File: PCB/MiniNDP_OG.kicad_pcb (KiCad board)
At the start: 2 copper layers, 60 x 34 mm, 27 parts, among them J1 Conn_02x20_Odd_Even, U1 HC161, U2 HC161, U3 HC161, U4 HC138, U5 HC574, U6 AS6C4008, U7 1G32, U8 1G79

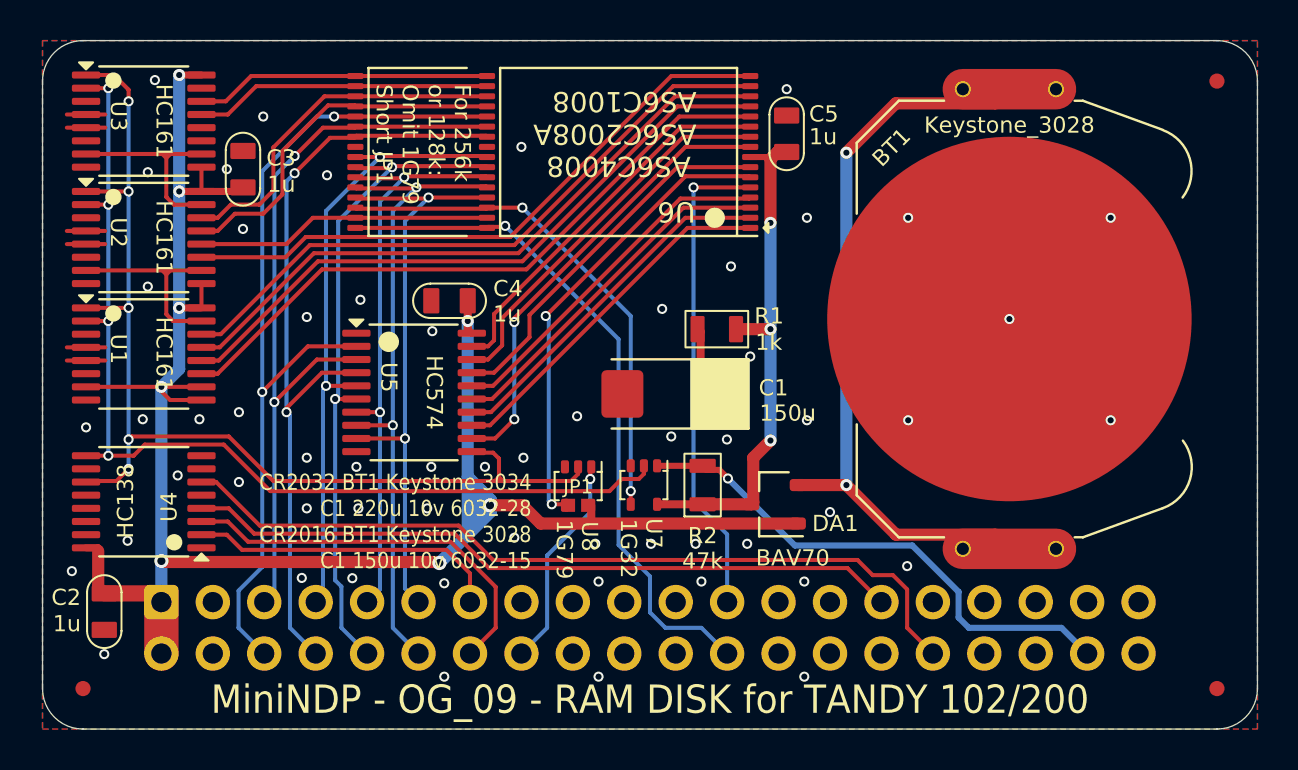
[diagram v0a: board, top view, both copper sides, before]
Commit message: minindp og orient bav70 for easier hand solder
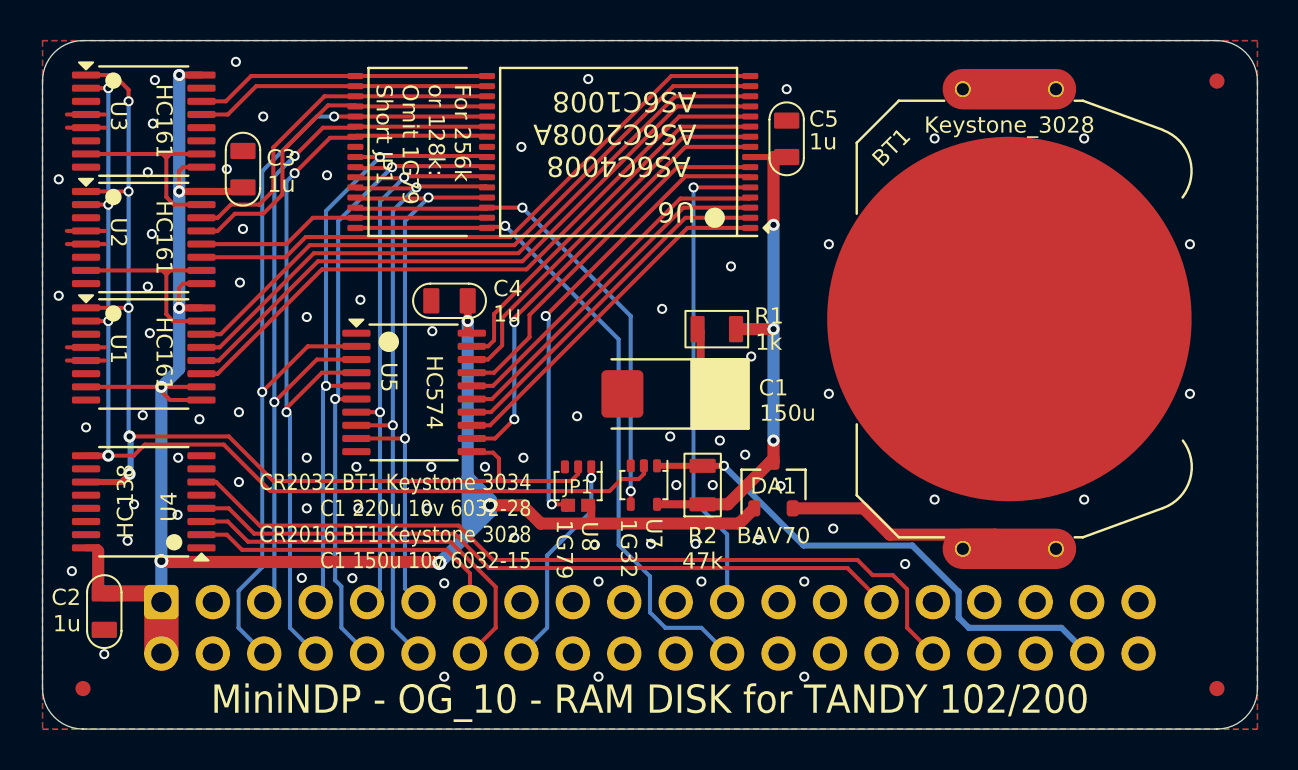
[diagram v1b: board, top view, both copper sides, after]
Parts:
- moved DA1 0.95 mm to (158.1, 108.0), turned to 90 degrees
- moved C5 0.25 mm to (158.7, 90.9)
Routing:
- net +BATT: track 37.5 -> 11.5 mm, vias 2 -> 0
- net VMEM: track 26.6 -> 25.3 mm
- net GND: vias 58 -> 73
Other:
- board text added: "bank0-1: P=129,133 block0-255: OUT P,N read byte: D=INP(131) write byte: OUT 131,D"
- board text removed: "bank0-1: P=129,133 block0-255: OUT P,N read byte: N=INP(131) write byte: OUT 131,N"

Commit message: OG fillet tracks
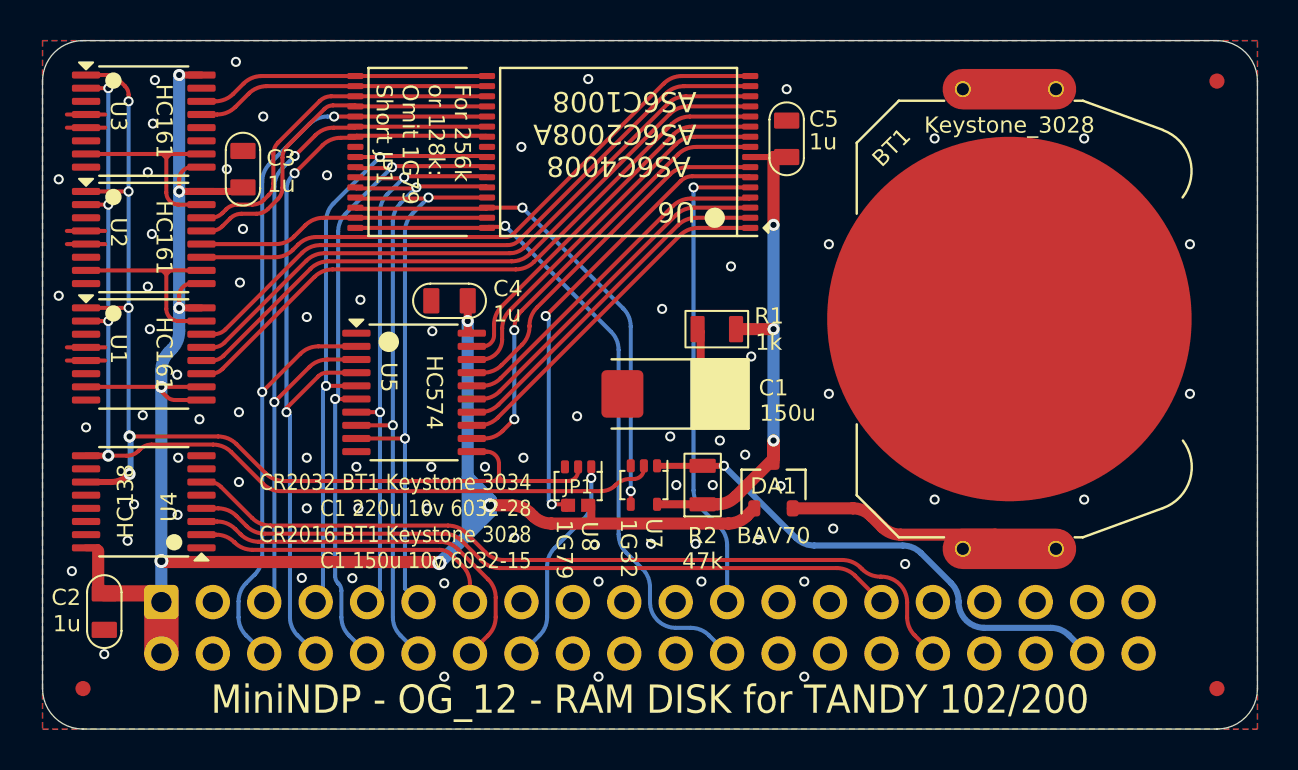
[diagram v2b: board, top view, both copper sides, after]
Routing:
- net VMEM: track 25.3 -> 26.2 mm
- net VBUS: track 96.3 -> 95.7 mm
- net /(A): track 40.7 -> 40.1 mm
- net /RAMRST: track 25.8 -> 25.3 mm
- net GND: vias 73 -> 74

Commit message: og traces & silkscreen
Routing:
- net GND: vias 74 -> 82
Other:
- board text added: "128K"
- board text added: "256K"
- board text added: "512K"
- board text added: "For 128k or 256k: Omit 1G79 Short JP1"
- board text removed: "For 256k or 128k: Omit 1G79 Short JP1"

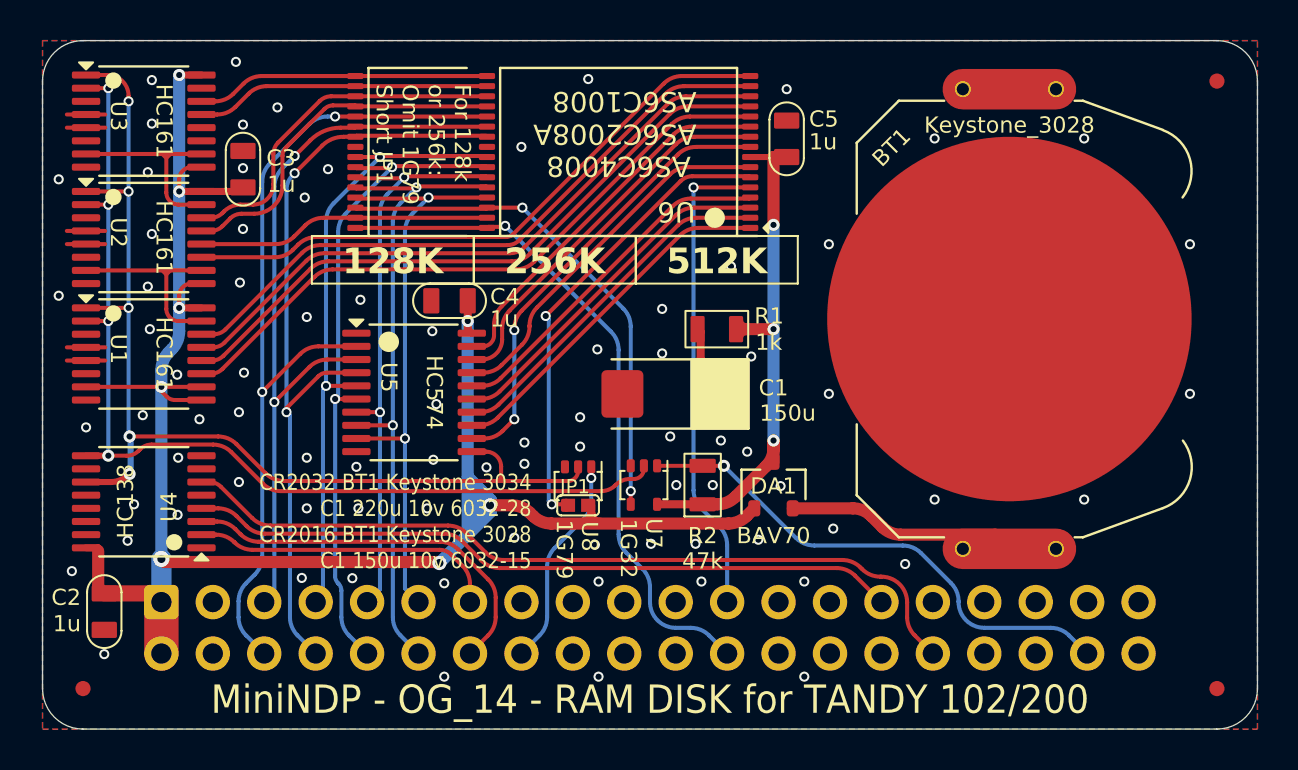
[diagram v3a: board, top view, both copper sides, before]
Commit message: ez256 compatible with 128k sram
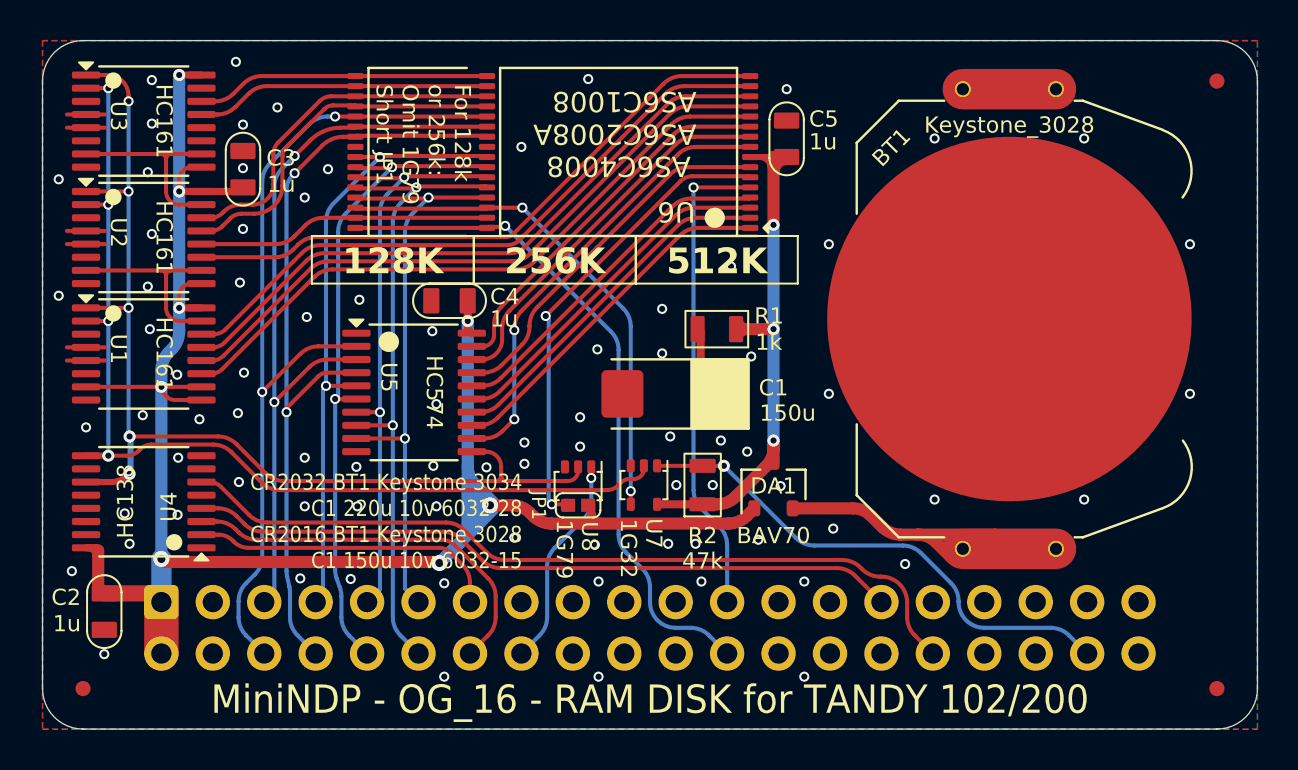
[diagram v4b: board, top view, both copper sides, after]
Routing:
- net VBUS: track 95.7 -> 99.3 mm
- net +BATT: track 11.4 -> 13.5 mm
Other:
- board text added: "BASIC to bootstrap RAMxxx.CO previously saved as the first file in bank 0"
- board text removed: "Bootstrap RAMDSK from BANK 0. For BANK 1 change OUT129 to OUT133. RAM100.CO or RAM200.CO must be the first file in the bank."

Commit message: battery holder footprints
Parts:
- removed REF** (x4): pth_nail, 000_LOCAL:pth_nail
- BT1: footprint 000_LOCAL:Keystone_3028_3034 -> 000_LOCAL:Keystone_3028_3034_bkw
- moved BT1 0.44 mm to (170.0, 99.5)
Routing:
- net +BATT: track 13.5 -> 11.6 mm
- net GND: vias 82 -> 74
